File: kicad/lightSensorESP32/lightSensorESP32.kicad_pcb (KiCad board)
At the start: 2 copper layers, 10 parts, among them SW1 SW_Push, U1 DHT11, U2 ESP32-BO

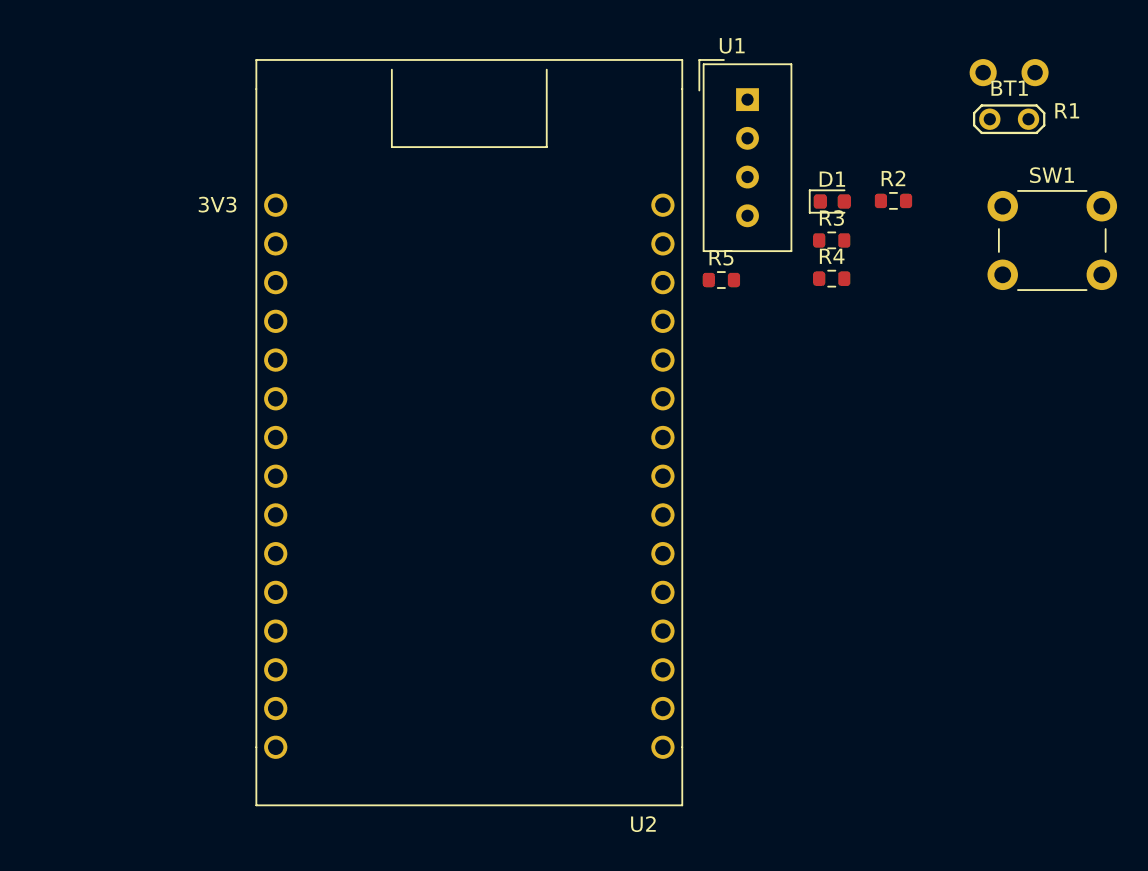
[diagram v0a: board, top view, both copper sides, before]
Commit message: Routed light, temperature, and humidity board and sent it off to be printed.
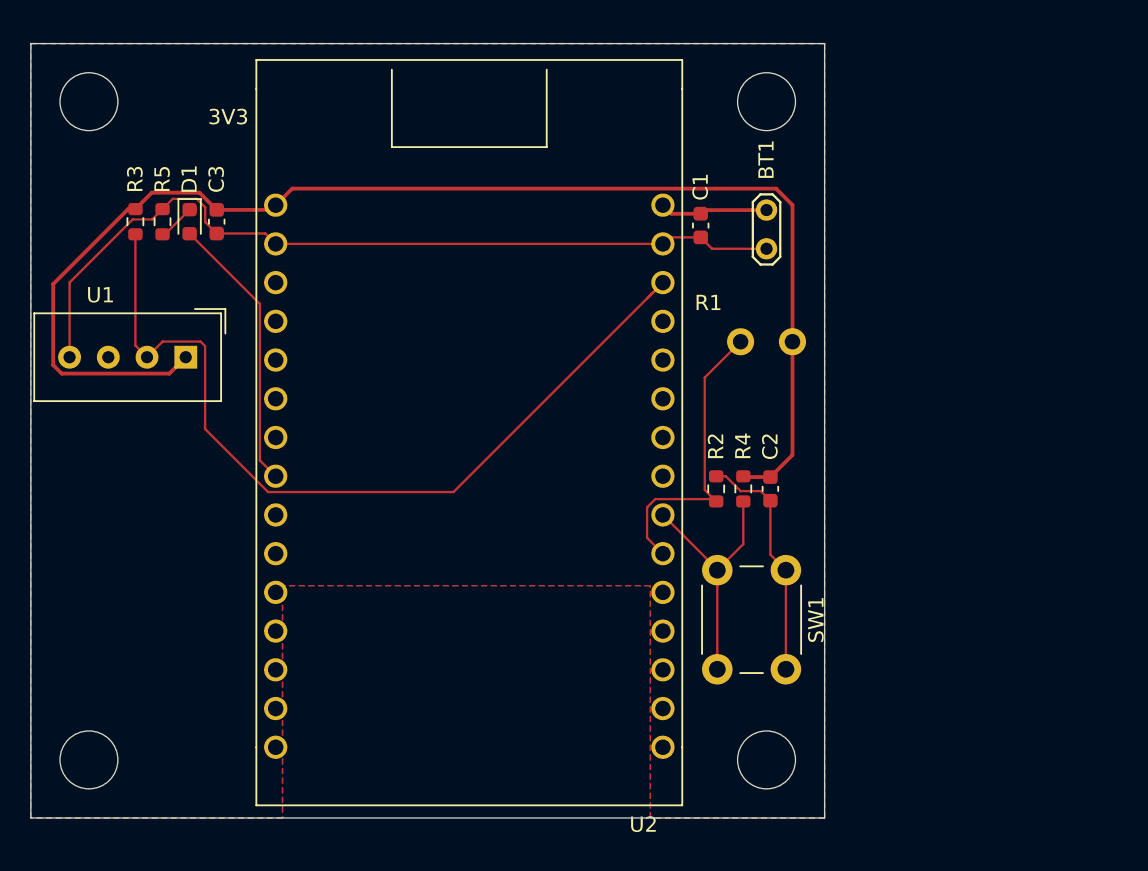
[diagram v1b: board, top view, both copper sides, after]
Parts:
- added C1: CAP, Capacitor_SMD:C_0603_1608Metric, F.Cu at (118.9, 61.5)
- added C2: CAP, Capacitor_SMD:C_0603_1608Metric, F.Cu at (123.4, 78.7)
- added C3: CAP, Capacitor_SMD:C_0603_1608Metric, F.Cu at (87.1, 61.2)
- moved R3 45.7 mm to (81.8, 61.2), turned to 270 degrees
- moved D1 42.2 mm to (85.3, 61.2), turned to 270 degrees
- moved U1 40.5 mm to (85.1, 70.1), turned to 270 degrees
- moved R5 36.9 mm to (83.6, 61.2), turned to 270 degrees
- moved SW1 27.8 mm to (124.5, 84.1), turned to 270 degrees
- moved R1 23.8 mm to (123.2, 69.1), turned to 180 degrees
- moved R2 22.2 mm to (119.9, 78.7), turned to 90 degrees
- moved BT1 15.8 mm to (123.2, 60.5), turned to 270 degrees
- moved R4 15.0 mm to (121.7, 78.7), turned to 90 degrees
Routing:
- net +3V3: track 0.00 -> 88.2 mm
- net GND: track 0.00 -> 70.9 mm
- net DHT: track 0.00 -> 57.1 mm
- net LGHT: track 0.00 -> 20.1 mm
- net LED: track 0.00 -> 18.2 mm
- net SWT: track 0.00 -> 16.8 mm
- net VCC: track 0.00 -> 7.13 mm
- net Net-(D1-Pad1): track 0.00 -> 2.45 mm
- added copper zone on F.Cu, net (none)
- added copper zone on B.Cu, net GND
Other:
- board outline added: 52.1 x 50.8 mm
